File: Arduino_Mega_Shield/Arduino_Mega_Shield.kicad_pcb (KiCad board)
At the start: 2 copper layers, 99.5 x 53.3 mm, 34 parts, among them J10 SW10, J11 SW6, J12 SW7, J13 SW8, J14 SW9, J18 Motor Driver Connector, J19 Screw_Terminal_01x02, J20 JOYSTICK, J21 I2C CONNECTOR, J22 ENCODER1, J26 I2C CONNECTOR, J3 Conn_01x04, J5 SW5, J6 SW1, J7 SW2, J8 SW3, J9 SW4

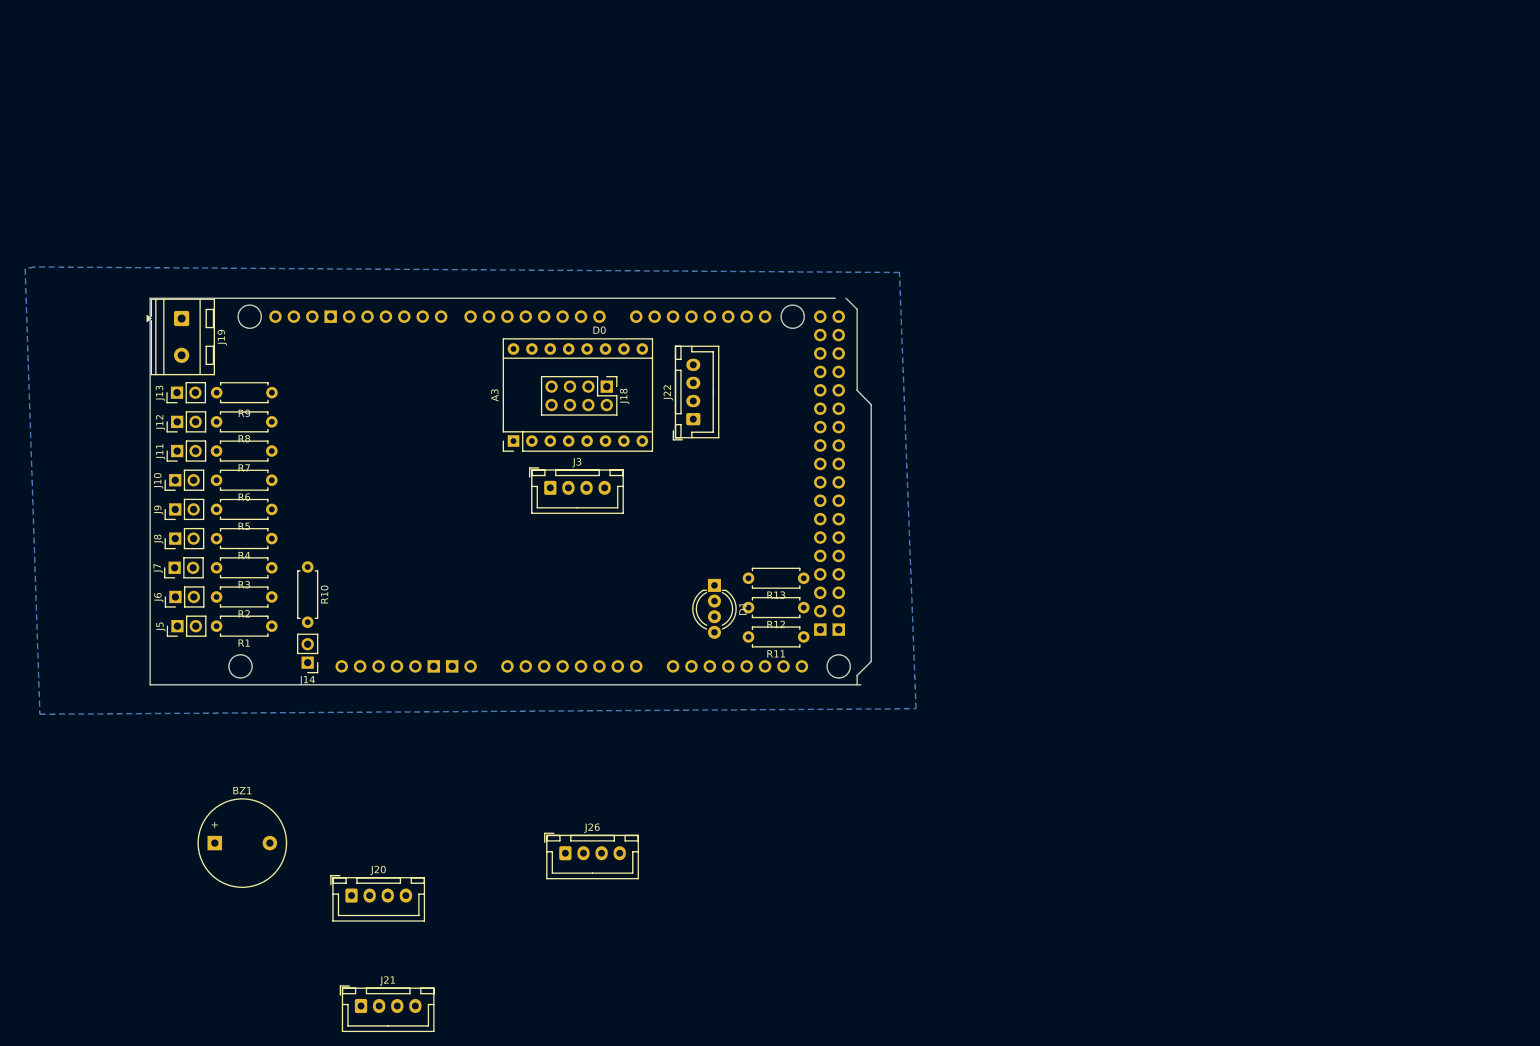
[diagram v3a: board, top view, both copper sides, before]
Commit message: Some mast modification before changing for a Arduino Mega
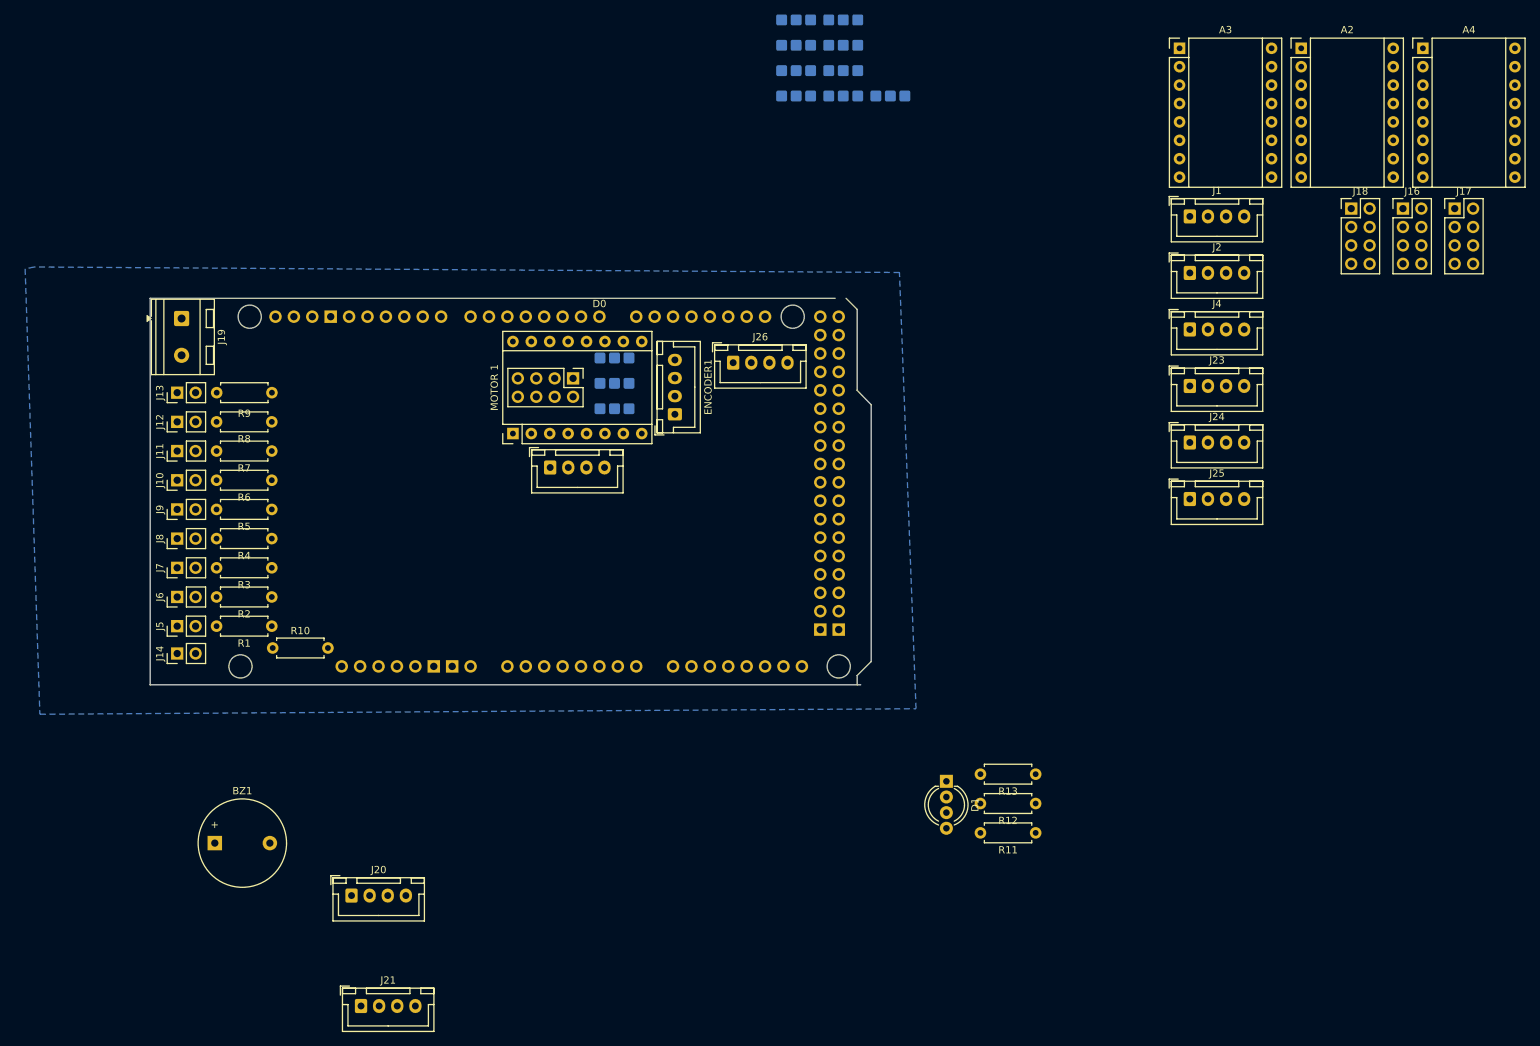
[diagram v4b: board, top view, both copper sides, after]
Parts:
- added A2: Pololu_Breakout_A4988, Module:Pololu_Breakout-16_15.2x20.3mm, F.Cu at (253.6, 29.0)
- added A3: Pololu_Breakout_A4988, Module:Pololu_Breakout-16_15.2x20.3mm, F.Cu at (236.8, 29.0)
- added A4: Pololu_Breakout_A4988, Module:Pololu_Breakout-16_15.2x20.3mm, F.Cu at (270.4, 29.0)
- added J1: Conn_01x04, Connector_JST:JST_XH_B4B-XH-A_1x04_P2.50mm_Vertical, F.Cu at (238.2, 52.2)
- added J16: Motor Driver Connector, Connector_PinHeader_2.54mm:PinHeader_2x04_P2.54mm_Vertical, F.Cu at (267.6, 51.1)
- added J17: Motor Driver Connector, Connector_PinHeader_2.54mm:PinHeader_2x04_P2.54mm_Vertical, F.Cu at (274.7, 51.1)
- added J18: Motor Driver Connector, Connector_PinHeader_2.54mm:PinHeader_2x04_P2.54mm_Vertical, F.Cu at (260.5, 51.1)
- added J2: Conn_01x04, Connector_JST:JST_XH_B4B-XH-A_1x04_P2.50mm_Vertical, F.Cu at (238.2, 60.0)
- added J23: ENCODER2, Connector_JST:JST_XH_B4B-XH-A_1x04_P2.50mm_Vertical, F.Cu at (238.2, 75.6)
- added J24: ENCODER3, Connector_JST:JST_XH_B4B-XH-A_1x04_P2.50mm_Vertical, F.Cu at (238.2, 83.4)
- added J25: ENCODER4, Connector_JST:JST_XH_B4B-XH-A_1x04_P2.50mm_Vertical, F.Cu at (238.2, 91.2)
- added J27: 3_pin_selector, Arduino MCU:3 pin selector, B.Cu at (158.8, 70.2)
- added J28: 3_pin_selector, Arduino MCU:3 pin selector, B.Cu at (158.8, 73.7)
- added J29: 3_pin_selector, Arduino MCU:3 pin selector, B.Cu at (158.8, 77.2)
- added J30: 3_pin_selector, Arduino MCU:3 pin selector, B.Cu at (196.9, 34.1)
- added J31: 3_pin_selector, Arduino MCU:3 pin selector, B.Cu at (190.4, 23.6)
- added J32: 3_pin_selector, Arduino MCU:3 pin selector, B.Cu at (190.4, 27.1)
- added J33: 3_pin_selector, Arduino MCU:3 pin selector, B.Cu at (190.4, 30.6)
- added J34: 3_pin_selector, Arduino MCU:3 pin selector, B.Cu at (190.4, 34.1)
- added J35: 3_pin_selector, Arduino MCU:3 pin selector, B.Cu at (183.9, 23.6)
- added J36: 3_pin_selector, Arduino MCU:3 pin selector, B.Cu at (183.9, 27.1)
- added J37: 3_pin_selector, Arduino MCU:3 pin selector, B.Cu at (183.9, 30.6)
- added J38: 3_pin_selector, Arduino MCU:3 pin selector, B.Cu at (183.9, 34.1)
- added J4: Conn_01x04, Connector_JST:JST_XH_B4B-XH-A_1x04_P2.50mm_Vertical, F.Cu at (238.2, 67.8)
- J26: value I2C CONNECTOR -> UART CONNECTOR
- MOTOR 1: renamed from A3
- moved J26 71.5 mm to (175.2, 72.4)
- moved D1 41.9 mm to (204.6, 130.2)
- moved R12 41.9 mm to (216.9, 133.2)
- moved R13 41.9 mm to (216.9, 129.2)
- moved R11 41.9 mm to (216.9, 137.3)
- moved J14 18.1 mm to (98.5, 112.5), turned to 90 degrees
- moved R10 12.2 mm to (111.6, 111.8), turned to 0 degrees
- moved J15 4.79 mm to (153.1, 74.6)
- moved J1 2.81 mm to (149.9, 86.9)
- moved J22 2.63 mm to (167.1, 79.5)
- moved MOTOR 1 1.03 mm to (144.8, 82.2)
- moved J7 0.34 mm to (98.5, 100.7)
- moved J10 0.27 mm to (98.5, 88.6)
- moved J8 0.27 mm to (98.5, 96.7)
- moved J9 0.27 mm to (98.5, 92.6)
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- renumbered J3 to J1, J18 to J15
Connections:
- A5 pad D2: unconnected-(A5-D2_INT0-PadD2) -> ENC_A1
- A5 pad D3: unconnected-(A5-D3_INT1-PadD3) -> ENC_A2
- J15 pad 1: RPWM4 -> RPWM1
- J15 pad 2: LPWM4 -> LPWM1
- J15 pad 3: R_EN4 -> R_EN1
- J15 pad 4: L_EN4 -> L_EN1
- J15 pad 5: R_IS4 -> R_IS1
- J15 pad 6: L_IS4 -> L_IS1
- MOTOR 1 pad 1: unconnected-(A3-GND-Pad1) -> GND
- MOTOR 1 pad 10: unconnected-(A3-MS1-Pad10) -> Net-(A1-MS1)
- MOTOR 1 pad 11: unconnected-(A3-MS2-Pad11) -> Net-(A1-MS2)
- MOTOR 1 pad 12: unconnected-(A3-MS3-Pad12) -> Net-(A1-MS3)
- MOTOR 1 pad 13: unconnected-(A3-~{RESET}-Pad13) -> R_IS1
- MOTOR 1 pad 14: unconnected-(A3-~{SLEEP}-Pad14) -> L_IS1
- MOTOR 1 pad 15: unconnected-(A3-STEP-Pad15) -> RPWM1
- MOTOR 1 pad 16: unconnected-(A3-DIR-Pad16) -> LPWM1
- MOTOR 1 pad 2: unconnected-(A3-VDD-Pad2) -> +5V
- MOTOR 1 pad 3: Net-(A3-1B) -> Net-(A1-1B)
- MOTOR 1 pad 4: Net-(A3-1A) -> Net-(A1-1A)
- MOTOR 1 pad 5: Net-(A3-2A) -> Net-(A1-2A)
- MOTOR 1 pad 6: Net-(A3-2B) -> Net-(A1-2B)
- MOTOR 1 pad 7: unconnected-(A3-GND-Pad7) -> GND
- MOTOR 1 pad 8: unconnected-(A3-VMOT-Pad8) -> +12V
- MOTOR 1 pad 9: unconnected-(A3-~{ENABLE}-Pad9) -> R_EN1
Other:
- board text added: "MS1"
- board text added: "MS2"
- board text added: "MS3"

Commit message: Avancement in the PCB design
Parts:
- removed the J1 at (238.2, 52.2)
- added J3: Conn_01x04, Connector_JST:JST_XH_B4B-XH-A_1x04_P2.50mm_Vertical, F.Cu at (140.3, 92.5)
- A1: renamed from MOTOR 1
- moved J17 158.4 mm to (125.1, 103.1), turned to -90 degrees
- moved A4 148.6 mm to (146.2, 110.7), turned to 90 degrees
- moved A3 145.1 mm to (116.8, 110.7), turned to 90 degrees
- moved A2 120.1 mm to (145.9, 82.2), turned to 90 degrees
- moved J18 118.0 mm to (154.5, 103.1), turned to -90 degrees
- moved J16 115.8 mm to (154.2, 74.6), turned to -90 degrees
- moved J24 102.0 mm to (139.2, 108.0), turned to 90 degrees
- moved J35 97.8 mm to (130.9, 105.8)
- moved J2 95.0 mm to (147.4, 88.0)
- moved J33 90.5 mm to (130.9, 98.8)
- moved J34 90.5 mm to (130.9, 102.3)
- moved J21 89.1 mm to (175.4, 88.5)
- moved J20 84.0 mm to (175.3, 80.5)
- moved BZ1 78.5 mm to (175.3, 106.7)
- moved J36 75.5 mm to (160.2, 98.8)
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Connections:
- A5 pad A10: unconnected-(A5-PadA10) -> SW3
- A5 pad A11: unconnected-(A5-PadA11) -> SW4
- A5 pad A12: unconnected-(A5-PadA12) -> SW5
- A5 pad A13: unconnected-(A5-PadA13) -> SW6
- A5 pad A14: unconnected-(A5-PadA14) -> SW7
- A5 pad A15: unconnected-(A5-PadA15) -> SW8
- A5 pad A8: unconnected-(A5-PadA8) -> SW1
- A5 pad A9: unconnected-(A5-PadA9) -> SW2
- A5 pad D12: RPWM4 -> SW9
- A5 pad D13: LPWM4 -> SW10
- A5 pad D18: ENC_A3 -> ENC_A2
- A5 pad D19: ENC_A4 -> ENC_B2
- A5 pad D3: ENC_A2 -> ENC_B1
- A5 pad D38: SW1 -> unconnected-(A5-PadD38)
- A5 pad D39: SW2 -> unconnected-(A5-PadD39)
- A5 pad D40: SW3 -> unconnected-(A5-PadD40)
- A5 pad D41: SW4 -> unconnected-(A5-PadD41)
- A5 pad D42: SW5 -> unconnected-(A5-PadD42)
- A5 pad D43: SW6 -> unconnected-(A5-PadD43)
- A5 pad D44: SW7 -> RPWM4
- A5 pad D45: SW8 -> LPWM4
- A5 pad D46: SW9 -> unconnected-(A5-PadD46)
- A5 pad D47: SW10 -> unconnected-(A5-PadD47)
- A5 pad D48: ENC_B1 -> unconnected-(A5-PadD48)
- A5 pad D49: ENC_B2 -> unconnected-(A5-PadD49)
- A5 pad D50: ENC_B3 -> ENC_A3
- A5 pad D51: ENC_B4 -> ENC_B3
- A5 pad D52: unconnected-(A5-D52_SCK-PadD52) -> ENC_A4
- A5 pad D53: unconnected-(A5-D53_CS-PadD53) -> ENC_B4
- J1 pad 1: Net-(A3-1B) -> Net-(A1-1B)
- J1 pad 2: Net-(A3-1A) -> Net-(A1-1A)
- J1 pad 3: Net-(A3-2A) -> Net-(A1-2A)
- J1 pad 4: Net-(A3-2B) -> Net-(A1-2B)
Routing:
- net +12V: track 0.00 -> 226.7 mm
- net +5V: track 0.00 -> 30.5 mm, vias 0 -> 10
- added copper zone on F.Cu, net +5V
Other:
- outline, holes or cut-outs redrawn
- copper layers 2 -> 4
- board text added: "Conn_01x04"
- board text added: "J2"

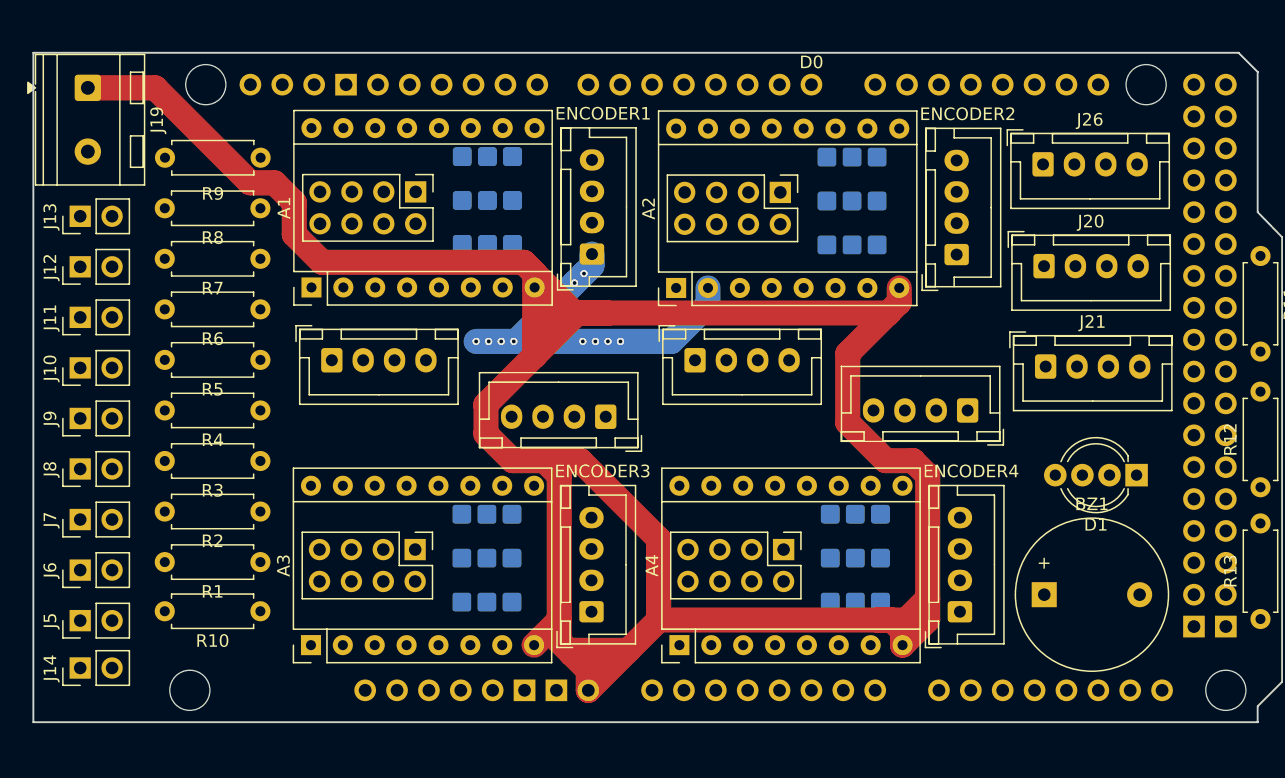
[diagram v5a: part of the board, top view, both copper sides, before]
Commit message: PCB trace, but not verified
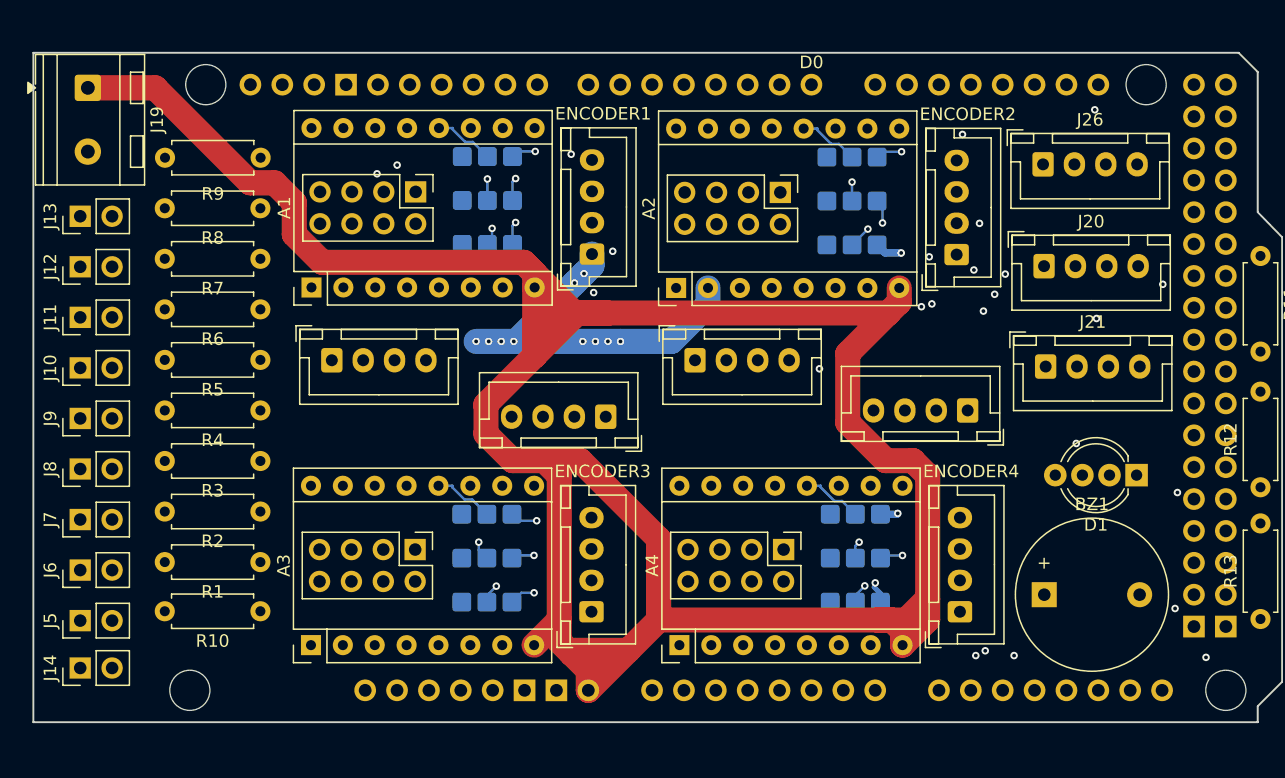
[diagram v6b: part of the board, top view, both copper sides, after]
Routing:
- net SW8: track 0.00 -> 123.5 mm, vias 0 -> 1
- net SW7: track 0.00 -> 114.1 mm, vias 0 -> 1
- net SW6: track 0.00 -> 109.6 mm, vias 0 -> 1
- net L_IS1: track 0.00 -> 95.9 mm
- net SDA: track 0.00 -> 94.2 mm
- net SCL: track 0.00 -> 93.8 mm
- net L_EN3: track 0.00 -> 90.5 mm, vias 0 -> 3
- net SW4: track 0.00 -> 90.0 mm, vias 0 -> 1
- net R_EN3: track 0.00 -> 87.3 mm, vias 0 -> 2
- net SW5: track 0.00 -> 86.5 mm
- net SW3: track 0.00 -> 86.1 mm, vias 0 -> 1
- net L_IS3: track 0.00 -> 83.3 mm
- net SW2: track 0.00 -> 83.2 mm, vias 0 -> 1
- net R_IS1: track 0.00 -> 79.7 mm, vias 0 -> 1
- net SW1: track 0.00 -> 77.6 mm
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
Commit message: First revision of the PCB
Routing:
- net +5V: track 53.6 -> 69.4 mm
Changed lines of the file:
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@@
 		)
 		(fp_line
-			(start 101 -3.2004)
+			(start 101 -3.21)
 			(end 101 -38.650256)
 			(stroke
@@
 		)
 		(fp_line
-			(start 101.2952 -3.0988)
+			(start 101.2952 -3.1242)
 			(end 101.2952 -38.8112)
 			(stroke
@@
 	)
 	(segment
+		(start 139.192 108.04)
+		(end 136.1307 108.04)
+		(width 0.2)
+		(layer "B.Cu")
+		(net 38)
+	)
+	(segment
 		(start 145.556 86.5)
 		(end 141.5 86.5)
@@
 	)
 	(segment
+		(start 146.078 108.04)
+		(end 148.738 110.7)
+		(width 0.2)
+		(layer "B.Cu")
+		(net 38)
+	)
+	(segment
 		(start 132 86.5)
 		(end 131 86.5)
@@
 	)
 	(segment
+		(start 139.192 108.04)
+		(end 146.078 108.04)
+		(width 0.2)
+		(layer "B.Cu")
+		(net 38)
+	)
+	(segment
 		(start 132.897 73.7721)
 		(end 132.897 75.271)
@@
 	)
 	(segment
+		(start 136.1307 108.04)
+		(end 134.6199 106.5292)
+		(width 0.2)
+		(layer "B.Cu")
+		(net 38)
+	)
+	(segment
 		(start 133.1481 77.021)
 		(end 132.897 77.2721)
@@
 	)
 	(via
-		(at 170.1117 77.0917)
+		(at 171 77.7885)
 		(size 0.6)
 		(drill 0.3)
@@
 	)
 	(segment
-		(start 128.27 92.8413)
-		(end 128.27 101.5943)
+		(start 140.8842 79.316)
+		(end 140.8842 80.2271)
 		(width 0.2)
 		(layer "In1.Cu")
@@
 	)
 	(segment
-		(start 167.533 78.2302)
-		(end 166.1038 79.6594)
+		(start 168.9732 78.2302)
+		(end 167.533 78.2302)
 		(width 0.2)
 		(layer "In1.Cu")
@@
 	)
 	(segment
-		(start 140.8842 79.316)
-		(end 140.8842 80.2271)
+		(start 123.809 104.418)
+		(end 122.602 105.625)
 		(width 0.2)
 		(layer "In1.Cu")
@@
 	)
 	(segment
-		(start 140.8842 80.2271)
-		(end 128.27 92.8413)
+		(start 126.582 104.418)
+		(end 123.809 104.418)
 		(width 0.2)
 		(layer "In1.Cu")
@@
 	)
 	(segment
-		(start 125.4463 104.418)
-		(end 123.809 104.418)
+		(start 169.4149 77.7885)
+		(end 168.9732 78.2302)
 		(width 0.2)
 		(layer "In1.Cu")
@@
 	)
 	(segment
-		(start 123.809 104.418)
-		(end 122.602 105.625)
+		(start 167.533 78.2302)
+		(end 166.1038 79.6594)
 		(width 0.2)
 		(layer "In1.Cu")
@@
 	)
 	(segment
-		(start 128.27 101.5943)
-		(end 125.4463 104.418)
+		(start 128.27 92.8413)
+		(end 128.27 102.73)
 		(width 0.2)
 		(layer "In1.Cu")
@@
 	)
 	(segment
-		(start 168.9732 78.2302)
-		(end 167.533 78.2302)
+		(start 171 77.7885)
+		(end 169.4149 77.7885)
 		(width 0.2)
 		(layer "In1.Cu")
@@
 	)
 	(segment
-		(start 170.1117 77.0917)
-		(end 168.9732 78.2302)
+		(start 140.8842 80.2271)
+		(end 128.27 92.8413)
 		(width 0.2)
 		(layer "In1.Cu")
@@
 	)
 	(segment
-		(start 190.905 75.7192)
-		(end 190.905 76.6805)
+		(start 128.27 102.73)
+		(end 126.582 104.418)
 		(width 0.2)
-		(layer "In2.Cu")
+		(layer "In1.Cu")
 		(net 52)
 	)
 	(segment
-		(start 141.6232 80.055)
-		(end 140.8842 79.316)
+		(start 171.4186 77.3699)
+		(end 190.2156 77.3699)
 		(width 0.2)
 		(layer "In2.Cu")
@@
 	(segment
 		(start 190.0111 74.8253)
-		(end 190.905 75.7192)
+		(end 189.738 74.8253)
 		(width 0.2)
 		(layer "In2.Cu")
@@
 	)
 	(segment
-		(start 165.8104 80.055)
-		(end 141.6232 80.055)
+		(start 141.6232 80.055)
+		(end 140.8842 79.316)
 		(width 0.2)
 		(layer "In2.Cu")
@@
 	)
 	(segment
-		(start 166.1038 79.7616)
-		(end 165.8104 80.055)
+		(start 190.2156 77.3699)
+		(end 190.905 76.6805)
 		(width 0.2)
 		(layer "In2.Cu")
@@
 	)
 	(segment
-		(start 170.3899 77.3699)
-		(end 170.1117 77.0917)
+		(start 190.905 76.6805)
+		(end 190.905 75.7192)
 		(width 0.2)
 		(layer "In2.Cu")
@@
 	)
 	(segment
-		(start 190.2156 77.3699)
-		(end 170.3899 77.3699)
+		(start 165.8104 80.055)
+		(end 141.6232 80.055)
 		(width 0.2)
 		(layer "In2.Cu")
@@
 	)
 	(segment
-		(start 190.905 76.6805)
-		(end 190.2156 77.3699)
+		(start 166.1038 79.7616)
+		(end 165.8104 80.055)
 		(width 0.2)
 		(layer "In2.Cu")
@@
 	)
 	(segment
-		(start 189.738 74.8253)
+		(start 190.905 75.7192)
 		(end 190.0111 74.8253)
 		(width 0.2)
@@
 	)
 	(segment
-		(start 189.738 73.66)
-		(end 189.738 74.8253)
+		(start 171 77.7885)
+		(end 171.4186 77.3699)
+		(width 0.2)
+		(layer "In2.Cu")
+		(net 52)
+	)
+	(segment
+		(start 189.738 74.8253)
+		(end 189.738 73.66)
 		(width 0.2)
 		(layer "In2.Cu")
@@
 		(layer "F.Cu")
 		(hatch edge 0.5)
-		(connect_pads
+		(connect_pads yes
 			(clearance 0.4)
 		)
